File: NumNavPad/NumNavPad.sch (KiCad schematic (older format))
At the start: 55 parts

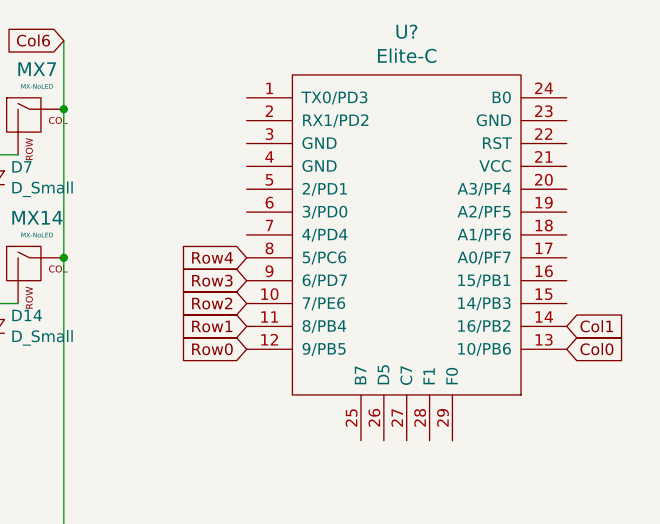
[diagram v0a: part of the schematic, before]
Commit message: Schematic and Pcb finished
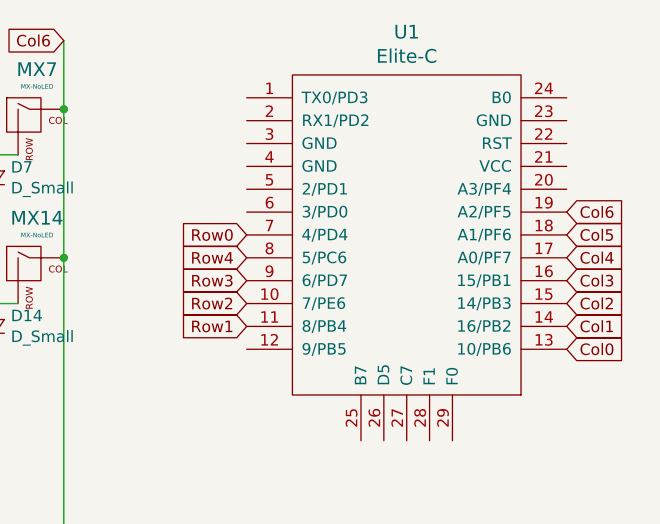
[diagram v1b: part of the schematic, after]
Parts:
- D1, D10, D11, D12, D13, D14, D15, D16, D17, D18, D19, D2, D20, D21, D22, D23, D24, D25, D26, D27, D3, D4, D5, D6, D7, D8, D9: footprint (none) -> keyboard_parts:D_SOD123_axial
- MX1, MX10, MX11, MX12, MX13, MX14, MX15, MX16, MX17, MX19, MX2, MX20, MX21, MX22, MX23, MX25, MX26, MX27, MX3, MX4, MX5, MX6, MX7, MX9: footprint (none) -> MX_Only:MXOnly-1U-NoLED
- MX18, MX8: footprint (none) -> MX_Only:MXOnly-2U-NoLED
- MX24: footprint (none) -> MX_Only:MXOnly-2U-ReversedStabilizers-NoLED
- U1: renamed from U?; footprint (none) -> Keebio-Parts:Elite-C-castellated-24pin-holes
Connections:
- net Col2: now also U1.15 (14/PB3)
- net Col3: now also U1.16 (15/PB1)
- net Col4: now also U1.17 (A0/PF7)
- net Col5: now also U1.18 (A1/PF6)
- net Col6: now also U1.19 (A2/PF5)
- net Row0: now also U1.7 (4/PD4); no longer U1.12 (9/PB5)

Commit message: Gerbers Added
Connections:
- net Col0: now also U1.19 (A2/PF5); no longer U1.13 (10/PB6)
- net Col1: now also U1.18 (A1/PF6); no longer U1.14 (16/PB2)
- net Col2: now also U1.17 (A0/PF7); no longer U1.15 (14/PB3)
- net Col4: now also U1.15 (14/PB3); no longer U1.17 (A0/PF7)
- net Col5: now also U1.6 (3/PD0); no longer U1.18 (A1/PF6)
- net Col6: now also U1.5 (2/PD1); no longer U1.19 (A2/PF5)
- net Row0: now also U1.20 (A3/PF4); no longer U1.7 (4/PD4)
- net Row1: now also U1.12 (9/PB5); no longer U1.11 (8/PB4)
- net Row2: now also U1.11 (8/PB4); no longer U1.10 (7/PE6)
- net Row3: now also U1.10 (7/PE6); no longer U1.9 (6/PD7)
- net Row4: now also U1.9 (6/PD7); no longer U1.8 (5/PC6)
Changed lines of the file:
@@
 	1    0    0    -1
 $EndComp
-Text GLabel 5100 1850 0    50   Input ~ 0
+Text GLabel 6500 1650 2    50   Input ~ 0
 Row0
+Text GLabel 5100 2350 0    50   Input ~ 0
+Row1
 Text GLabel 5100 2250 0    50   Input ~ 0
-Row1
+Row2
 Text GLabel 5100 2150 0    50   Input ~ 0
-Row2
+Row3
 Text GLabel 5100 2050 0    50   Input ~ 0
-Row3
-Text GLabel 5100 1950 0    50   Input ~ 0
 Row4
-Text GLabel 6500 2350 2    50   Input ~ 0
+Text GLabel 6500 1750 2    50   Input ~ 0
 Col0
-Text GLabel 6500 2250 2    50   Input ~ 0
+Text GLabel 6500 1850 2    50   Input ~ 0
 Col1
-Text GLabel 6500 2150 2    50   Input ~ 0
+Text GLabel 6500 1950 2    50   Input ~ 0
 Col2
 Text GLabel 6500 2050 2    50   Input ~ 0
 Col3
-Text GLabel 6500 1950 2    50   Input ~ 0
+Text GLabel 6500 2150 2    50   Input ~ 0
 Col4
-Text GLabel 6500 1850 2    50   Input ~ 0
+Text GLabel 5100 1750 0    50   Input ~ 0
 Col5
-Text GLabel 6500 1750 2    50   Input ~ 0
+Text GLabel 5100 1650 0    50   Input ~ 0
 Col6
 $EndSCHEMATC
